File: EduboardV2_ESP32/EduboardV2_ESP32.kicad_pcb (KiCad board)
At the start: 4 copper layers, 35 x 63.3 mm, 89 parts, among them J1 EduboardV2 PCIE UP Board Conn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, Q1 S8050_C139514, Q2 S8050_C139514, Q3 AO3401A, SW1 K2-1102SP-C4SC-04, SW2 K2-1102SP-C4SC-04, U1 ESP32-WROOM-E, U2 FT2232HL, U3 M93C46-WMN6TP, U4 SX1509BIULTRT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

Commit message: finalize Data. Add Logo and Text
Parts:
- added G***: LOGO, EduboardV2_kicadlib:JuventusLogo, F.Cu at (116.5, 114.0)
- moved D3 4.20 mm to (113.4, 107.8), turned to 0 degrees
- moved R30 1.14 mm to (116.8, 111.6), turned to 90 degrees
- moved D2 0.60 mm to (115.7, 107.8)
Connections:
- net Net-(U2-DM) renamed /DebugChip FT2232HL/D_N
- net Net-(U2-DP) renamed /DebugChip FT2232HL/D_P
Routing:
- net D-: track 16.1 -> 12.8 mm, vias 0 -> 2
- net USB_Debug_D-: track 52.3 -> 54.8 mm
- net GND: track 115.6 -> 117.5 mm
- net Net-(U2-VPLL): track 8.40 -> 10.1 mm
- net USB_Debug_D+: track 59.8 -> 58.2 mm
- net D+: track 12.0 -> 13.0 mm
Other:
- board text added: "Eduboard 2 UP-Board ESP32 V${HW_VERSION}"

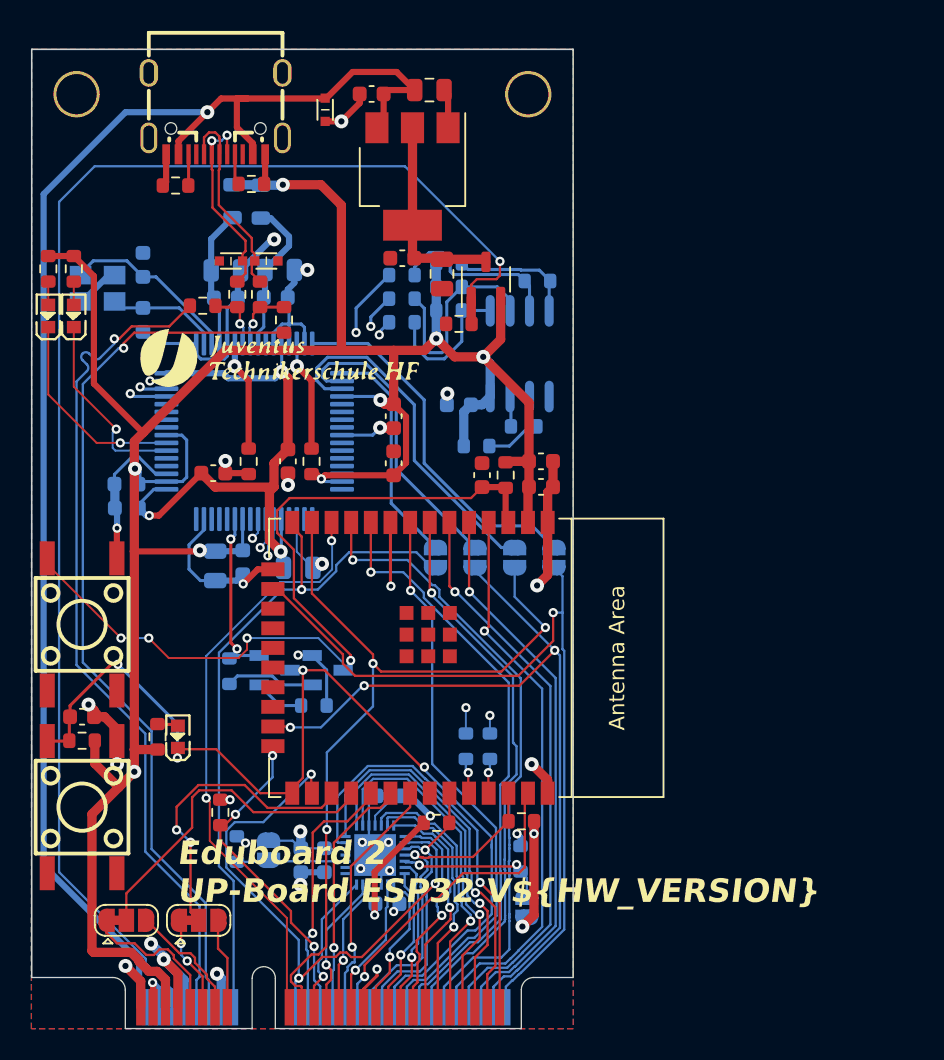
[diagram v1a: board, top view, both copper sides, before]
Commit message: add gnd vias. Improve USB Diff Line. Work on finalization of pcb
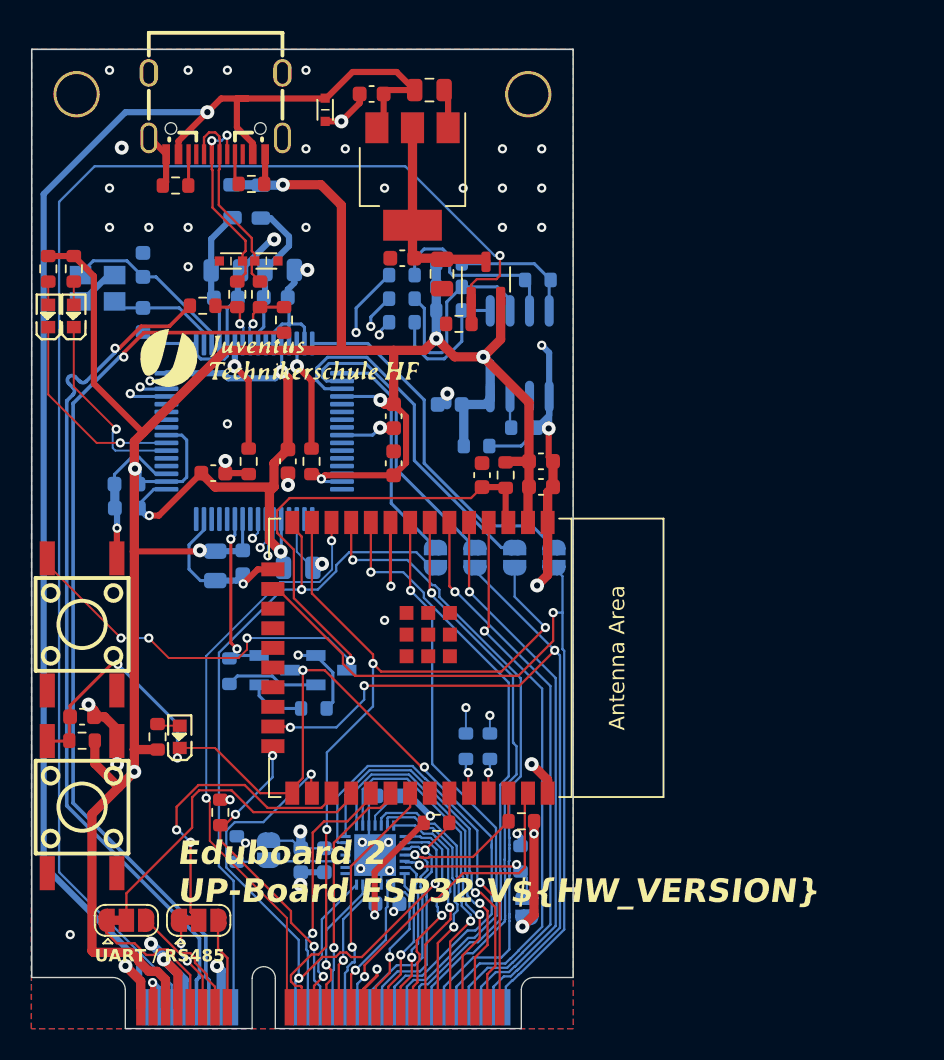
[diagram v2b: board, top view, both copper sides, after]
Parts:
- moved C3 0.59 mm to (127.5, 117.1)
- moved Q1 0.24 mm to (119.9, 134.3)
- moved R18 0.19 mm to (118.8, 136.8)
- moved LED3 0.12 mm to (110.1, 138.6)
- moved R21 0.09 mm to (132.3, 118.6)
- moved R1 0.07 mm to (133.2, 109.0)
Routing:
- net GND: track 117.5 -> 129.7 mm, vias 27 -> 53
- net EEDATA: track 11.3 -> 12.0 mm
- net FT_nRTS: track 14.7 -> 15.4 mm
- net +3V3: track 228.3 -> 228.9 mm
- net ESP_TDO: track 53.1 -> 53.6 mm
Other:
- board text added: "0"
- board text added: "1"
- board text added: "Debug"
- board text added: "UART / RS485"
